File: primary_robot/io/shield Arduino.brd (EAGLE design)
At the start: 64.1 x 81.3 mm, 40 parts

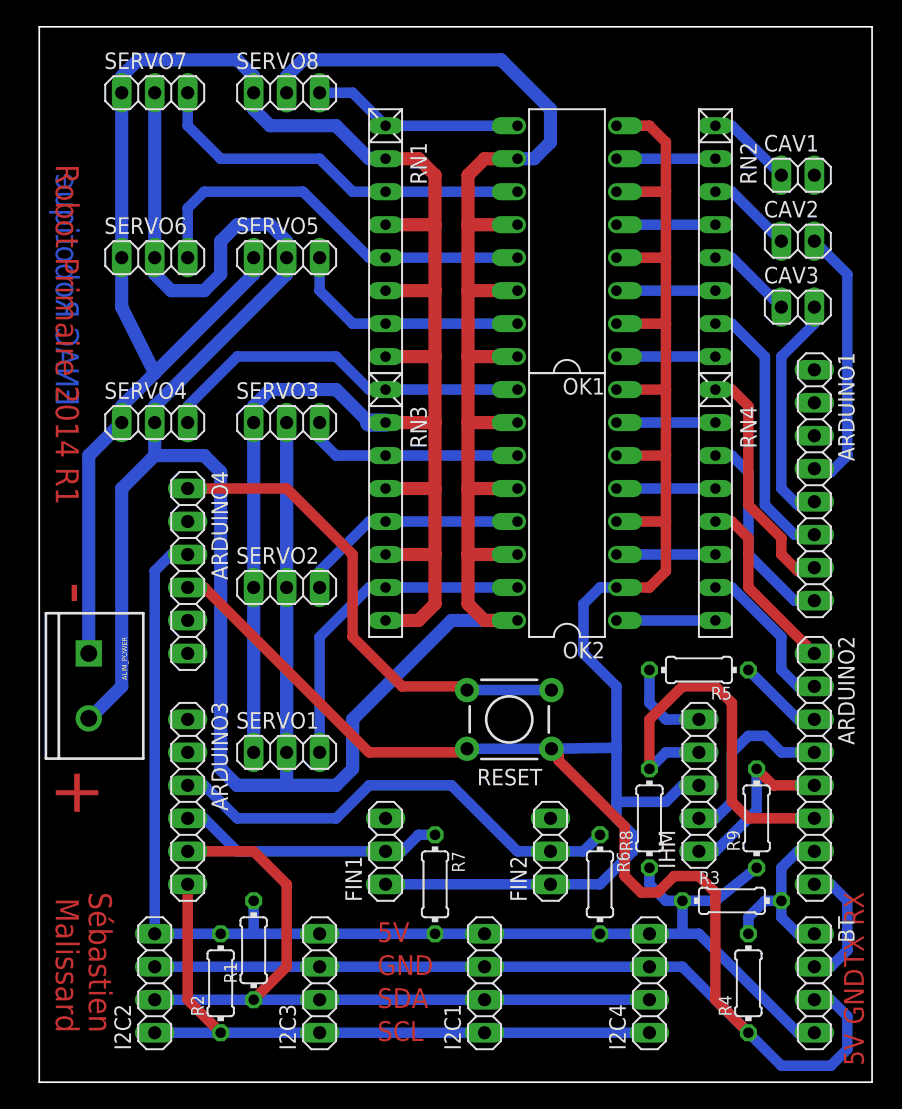
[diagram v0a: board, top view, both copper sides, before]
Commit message: [priom/io] Updates some labels
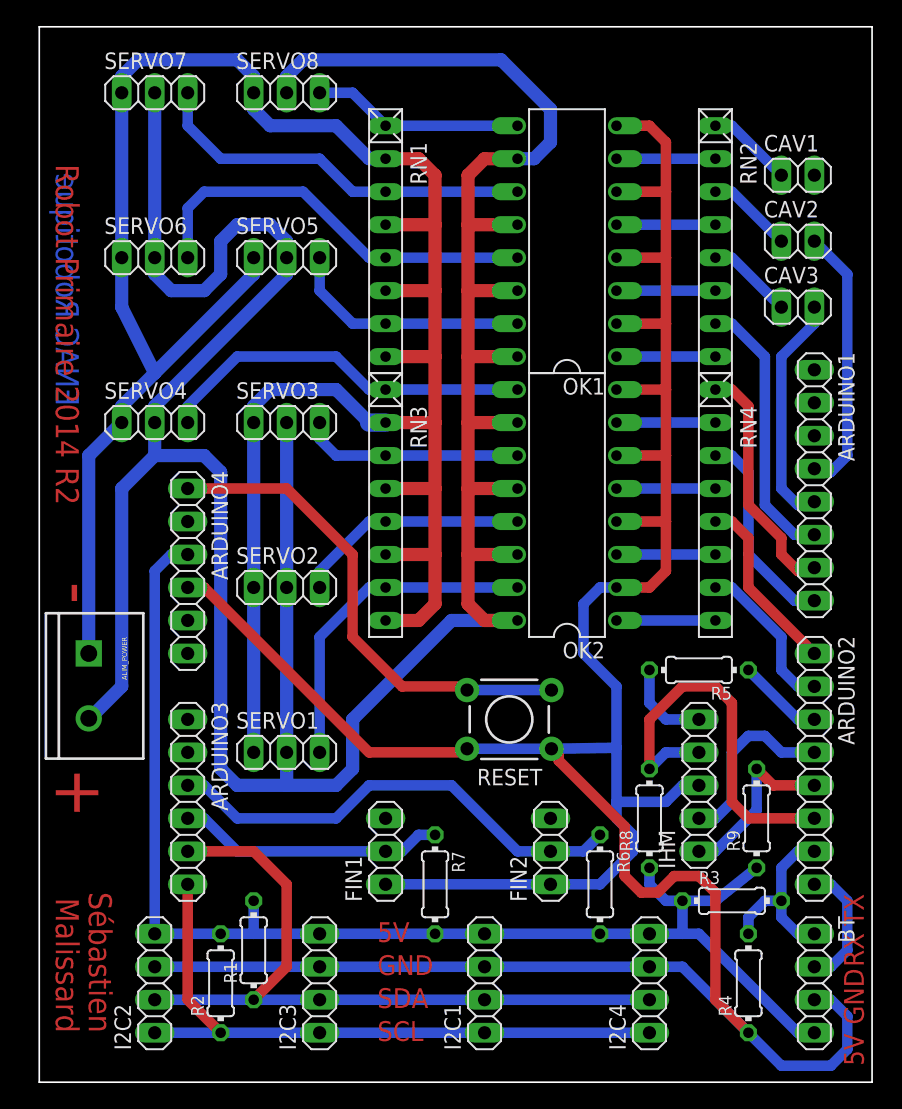
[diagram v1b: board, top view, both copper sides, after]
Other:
- board text added: "Robot Primaire 2014 R2"
- board text removed: "Robot Primaire 2014 R1"
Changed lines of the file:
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@@
 <wire x1="15.24" y1="82.55" x2="79.375" y2="82.55" width="0.127" layer="20"/>
 <wire x1="79.375" y1="1.27" x2="79.375" y2="82.55" width="0.127" layer="20"/>
-<text x="16.51" y="45.72" size="1.778" layer="1" font="vector" ratio="15" rot="SR270" align="bottom-right">Robot Primaire 2014 R1</text>
+<text x="16.51" y="45.72" size="1.778" layer="1" font="vector" ratio="15" rot="SR270" align="bottom-right">Robot Primaire 2014 R2</text>
 <text x="19.05" y="5.08" size="1.778" layer="1" font="vector" ratio="15" rot="SR270" align="bottom-right">Sébastien</text>
 <text x="16.51" y="21.59" size="3.81" layer="1" font="vector" ratio="20" rot="SR270" align="bottom-right">+</text>
@@
 <text x="41.275" y="9.525" size="1.524" layer="1" font="vector" ratio="15" rot="SR0">GND</text>
 <text x="41.275" y="12.065" size="1.524" layer="1" font="vector" ratio="15" rot="SR0">5V</text>
-<text x="78.74" y="13.335" size="1.524" layer="1" font="vector" ratio="15" rot="SR90">RX</text>
-<text x="78.74" y="10.16" size="1.524" layer="1" font="vector" ratio="15" rot="SR90">TX</text>
+<text x="78.74" y="13.335" size="1.524" layer="1" font="vector" ratio="15" rot="SR90">TX</text>
+<text x="78.74" y="10.16" size="1.524" layer="1" font="vector" ratio="15" rot="SR90">RX</text>
 <text x="78.74" y="5.715" size="1.524" layer="1" font="vector" ratio="15" rot="SR90">GND</text>
 <text x="78.74" y="2.54" size="1.524" layer="1" font="vector" ratio="15" rot="SR90">5V</text>
